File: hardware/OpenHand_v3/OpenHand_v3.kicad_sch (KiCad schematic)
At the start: 59 parts, among them J1 CONN_MOTOR_1, J11 CONN_EMG_2, J12 CONN_SWD, J14 CONN_MOTOR_1_ENCODER, J15 CONN_MOTOR_2_ENCODER, J16 CONN_MOTOR_3_ENCODER, J2 CONN_MOTOR_2, J3 CONN_BATT, J5 CONN_USB_C, J6 CONN_MOTOR_3, J7 CONN_FDBK, J8 CONN_EMG_1, SW1 BTN_RST, SW2 SW_Push, U1 STM32F103RETx, Y1 16MHz

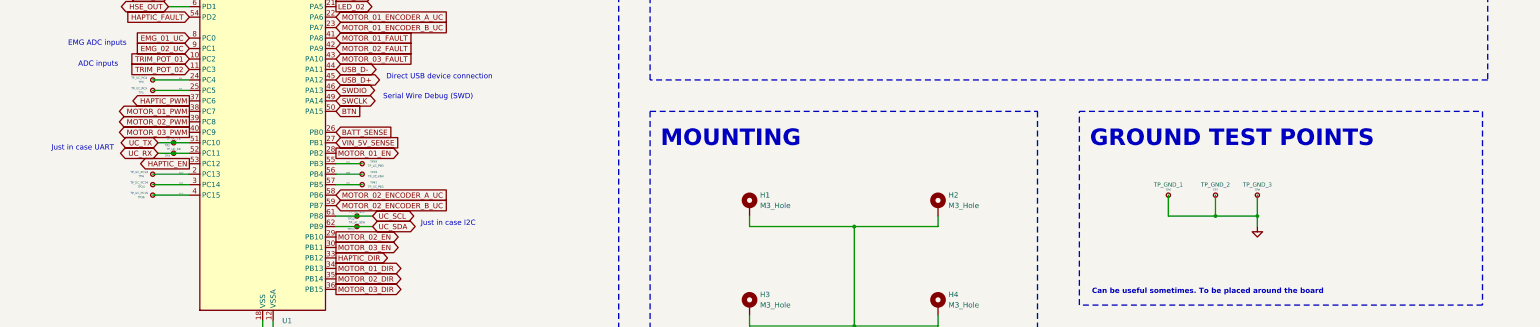
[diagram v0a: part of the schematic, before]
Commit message: Update PCB via size, start with code infrastructure idea
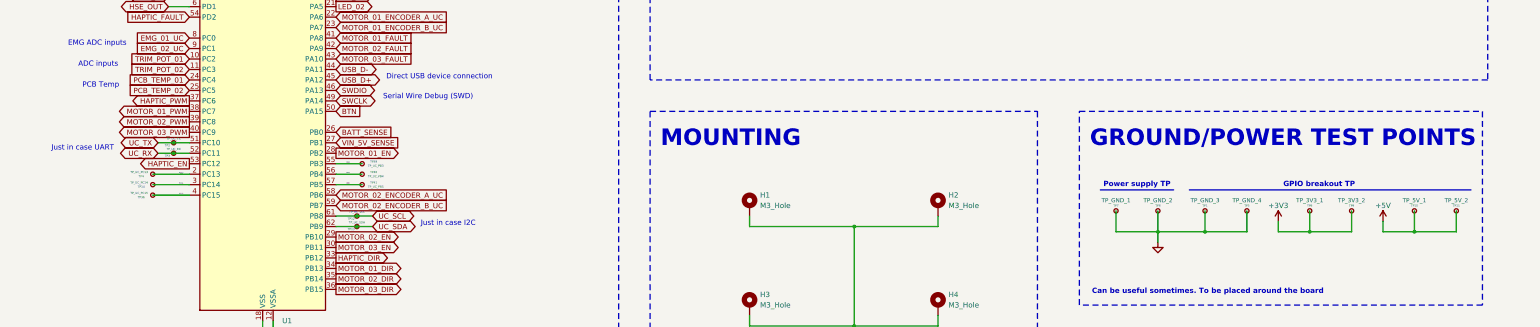
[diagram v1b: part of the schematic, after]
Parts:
- added TP10: TP_5V_1, TestPoint:TestPoint_THTPad_D1.5mm_Drill0.7mm, symbol Connector:TestPoint_Small
- added TP11: TP_5V_2, TestPoint:TestPoint_THTPad_D1.5mm_Drill0.7mm, symbol Connector:TestPoint_Small
- added TP9: TP_3V3_2, TestPoint:TestPoint_THTPad_D1.5mm_Drill0.7mm, symbol Connector:TestPoint_Small
- TP1: value TP_UC_PC5 -> TP_GND_3
- TP5: value TP_UC_PC4 -> TP_GND_4
- TP6: value TP_GND_1 -> TP_3V3_1
- TP7: value TP_GND_2 -> TP_GND_1
- TP8: value TP_GND_3 -> TP_GND_2
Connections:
- net +3V3: now also TP6.1, TP9.1
- net +5V: now also TP10.1, TP11.1
- net GND: now also TP1.1, TP5.1; no longer TP6.1
- net PC4 renamed PCB_TEMP_01
- net PCB_TEMP_01: no longer TP5.1
- net PC5 renamed PCB_TEMP_02
- net PCB_TEMP_02: no longer TP1.1
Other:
- note added: "GPIO breakout TP"
- note added: "GROUND/POWER TEST POINTS"
- note added: "PCB Temp"
- note added: "Power supply TP"
- note removed: "GROUND TEST POINTS"
- moved on the sheet: TP7, TP8
